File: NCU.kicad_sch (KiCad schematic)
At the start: 3 parts, among them J2 USB_C_Receptacle_USB2.0_14P

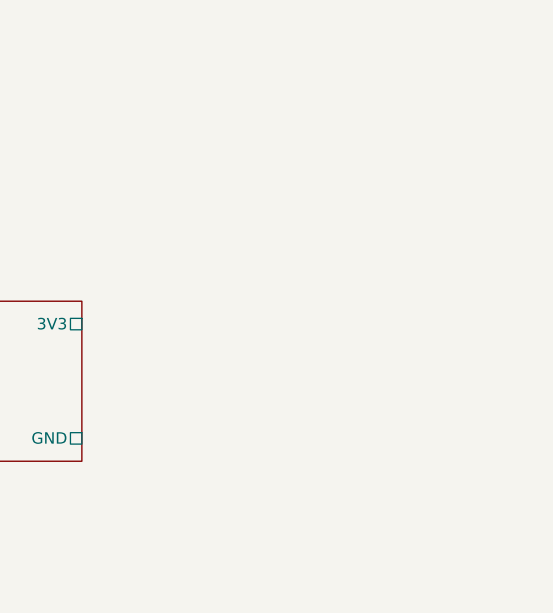
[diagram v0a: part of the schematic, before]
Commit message: added ethernet chip
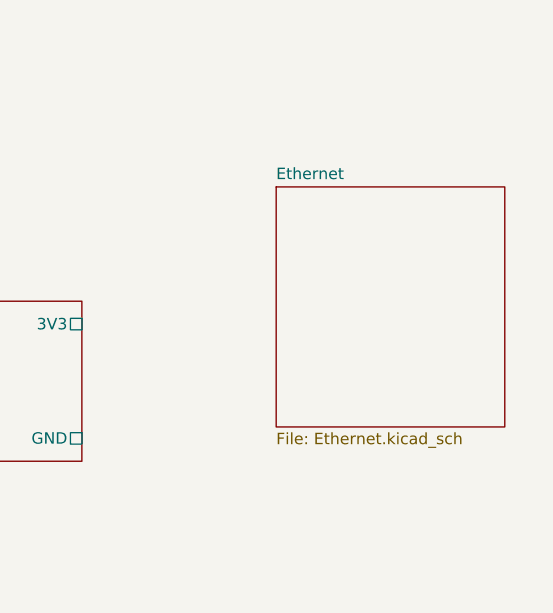
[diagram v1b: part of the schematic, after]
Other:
- added sheet Ethernet (Ethernet.kicad_sch)
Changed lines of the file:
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@@
+	)
+	(sheet
+		(at 228.6 63.5)
+		(size 25.4 26.67)
+		(exclude_from_sim no)
+		(in_bom yes)
+		(on_board yes)
+		(dnp no)
+		(fields_autoplaced yes)
+		(stroke
+			(width 0.1524)
+			(type solid)
+		)
+		(fill
+			(color 0 0 0 0.0000)
+		)
+		(property "Sheetname" "Ethernet"
+			(at 228.6 62.7884 0)
+			(effects
+				(font
+					(size 1.27 1.27)
+				)
+				(justify left bottom)
+			)
+		)
+		(property "Sheetfile" "Ethernet.kicad_sch"
+			(at 228.6 90.7546 0)
+			(effects
+				(font
+					(size 1.27 1.27)
+				)
+				(justify left top)
+			)
+		)
+		(instances
+			(project "NCU"
+				(path "/3aee14c3-5480-4f7c-989e-3fef81779034"
+					(page "8")
+				)
+			)
+		)
 	)
 	(sheet

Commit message: wip
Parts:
- removed J2: USB_C_Receptacle_USB2.0_14P, Connector_USB:USB_C_Receptacle_GCT_USB4110, symbol Connector:USB_C_Receptacle_USB2.0_14P
- removed R1, R2: 5K1, symbol Device:R
- added J1: RJ45, Connector_RJ:RJ45_Hanrun_HR911105A_Horizontal, symbol Connector:RJ45
- added J2: USB_B, symbol Connector:USB_B
- added J3: Micro_SD_Card, Connector_Card:microSD_HC_Molex_47219-2001, symbol Connector:Micro_SD_Card
- added J4: USB_C_Receptacle, symbol Connector:USB_C_Receptacle
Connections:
- net +5V: now also J2.1 (VBUS)
- net GND: now also J2.4 (GND), J2.5 (Shield), J3.9 (SHIELD)
- net USB/D+: now also J2.2 (D-)
- net USB/D-: now also J2.3 (D+)
- new net: J4.A1 (GND), J4.A12 (GND), J4.B1 (GND), J4.B12 (GND)
- new net: J4.A4 (VBUS), J4.A9 (VBUS), J4.B4 (VBUS), J4.B9 (VBUS)
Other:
- sheet Wireless Module renamed WiFi Bluetooth Module
- added sheet Cellular Module (CellularModule.kicad_sch)
- sheet WiFi Bluetooth Module: file WirelessModule.kicad_sch -> WifiBluetoothModule.kicad_sch

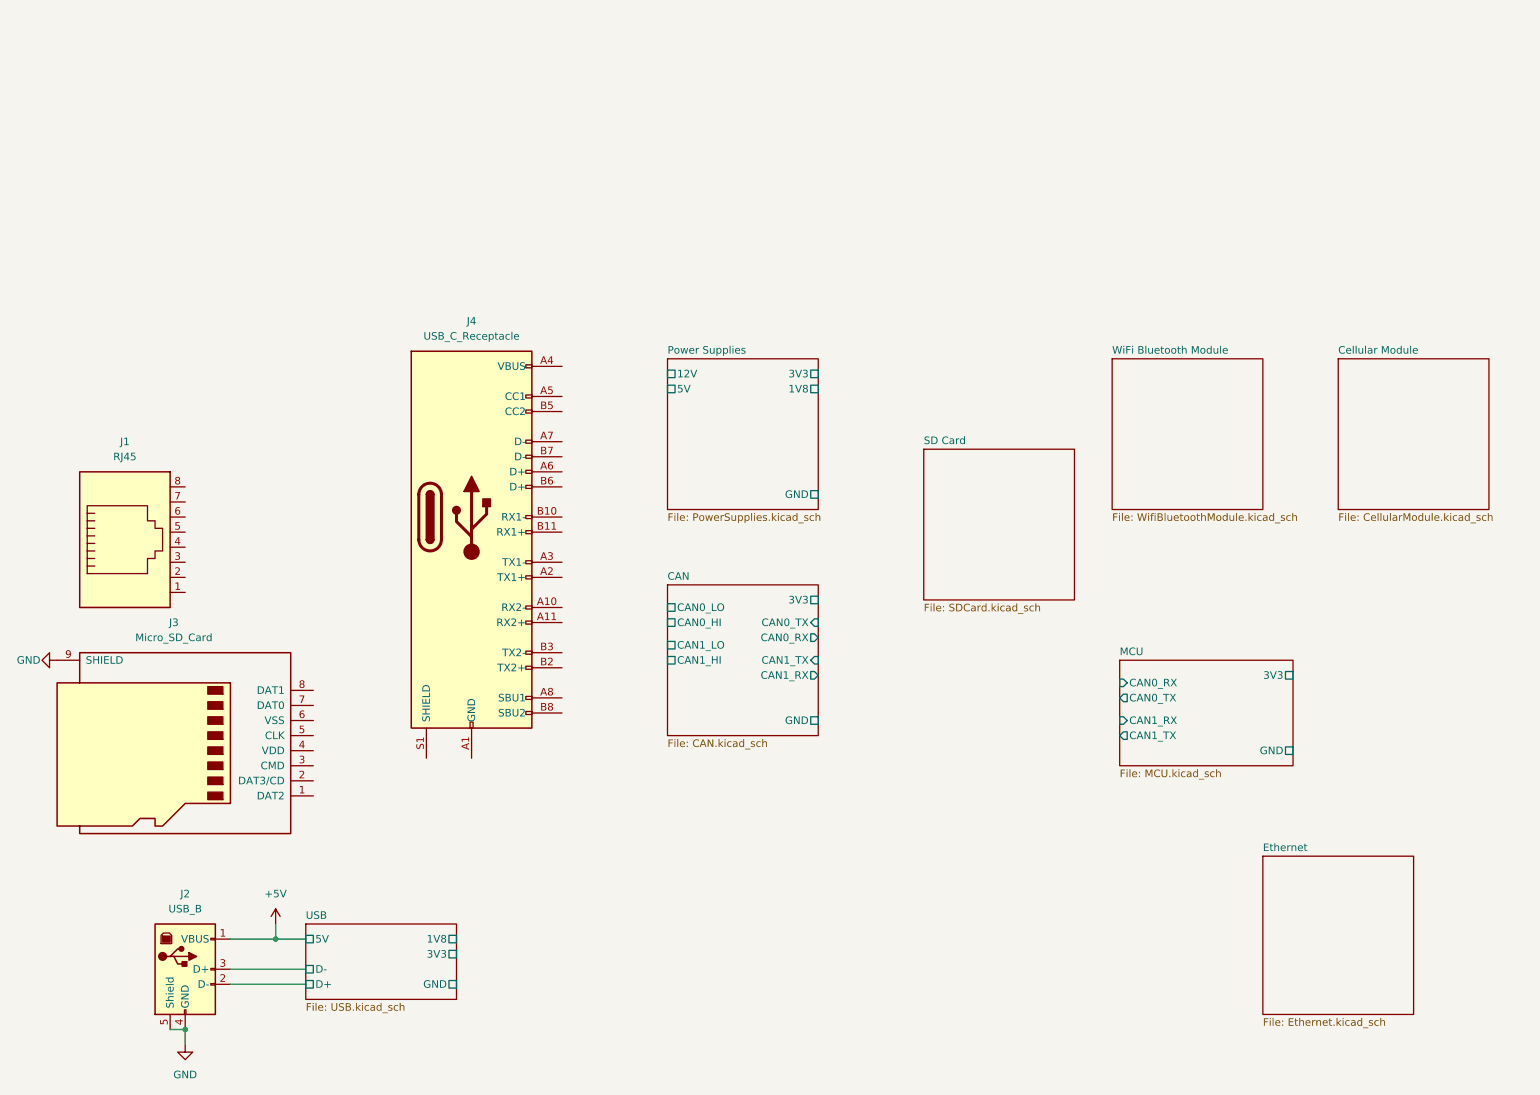
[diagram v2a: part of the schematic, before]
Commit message: updated to use RMII and routed ethernet and CAN from micro
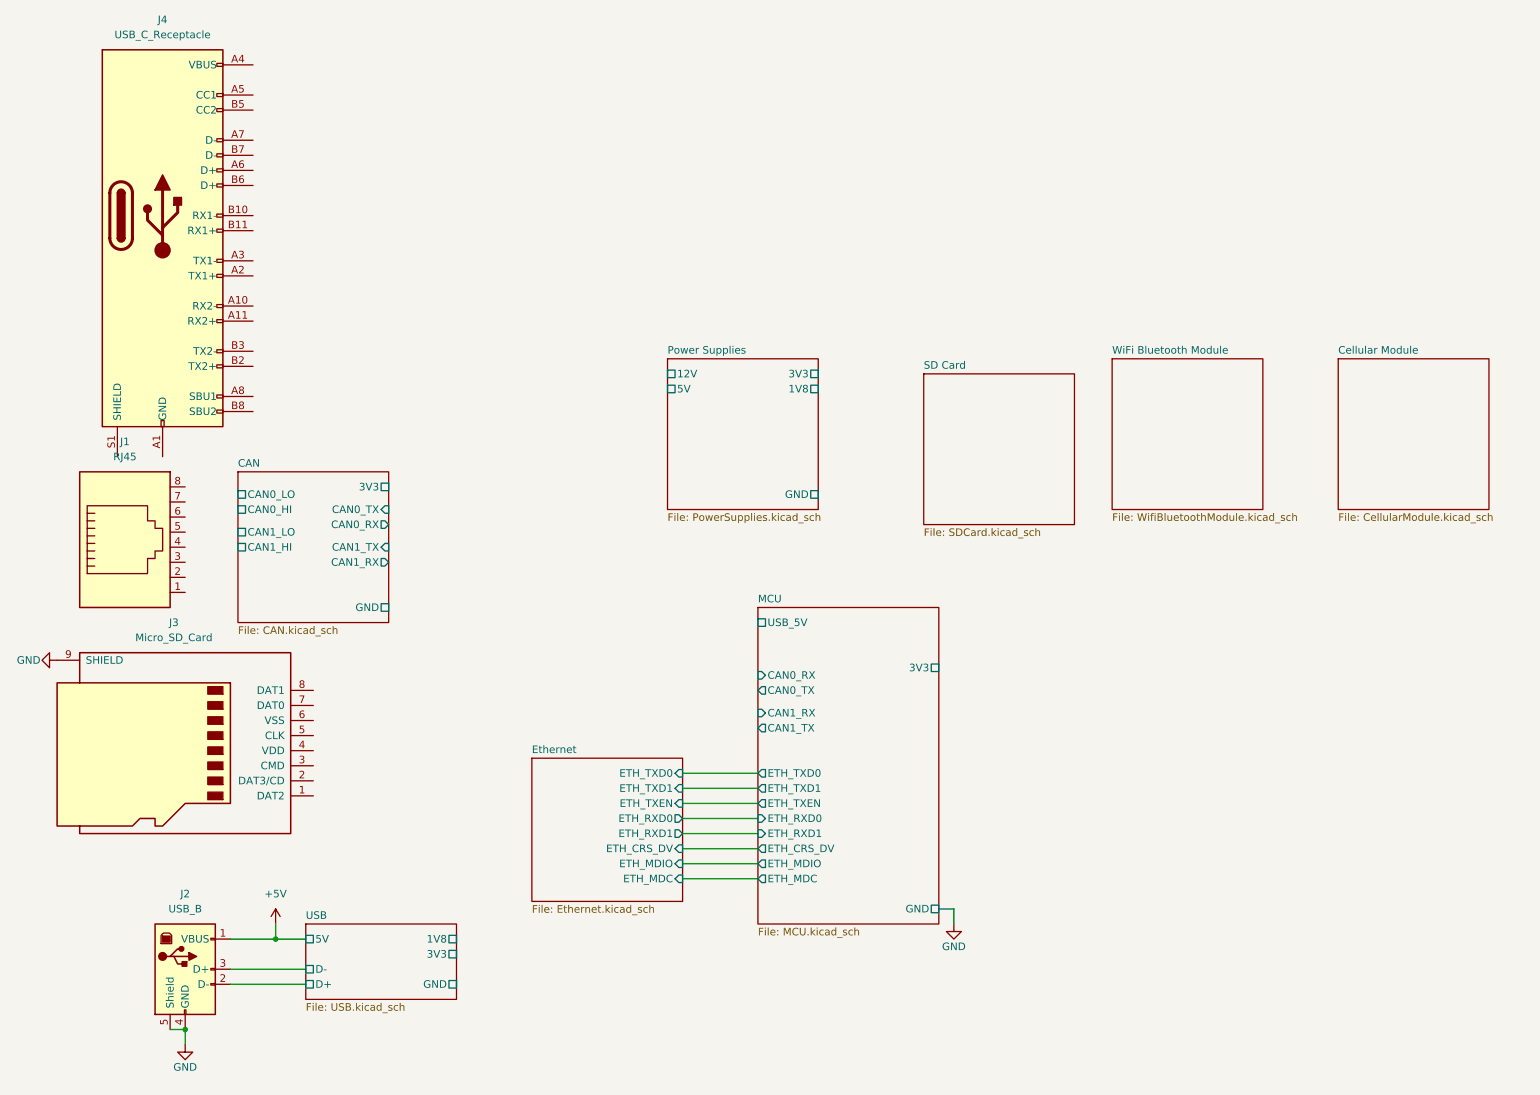
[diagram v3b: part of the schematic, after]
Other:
- sheet Ethernet ports: added ETH_CRS_DV, ETH_MDC, ETH_MDIO, ETH_RXD0, ETH_RXD1, ETH_TXD0, ETH_TXD1, ETH_TXEN; removed none
- sheet MCU ports: added ETH_CRS_DV, ETH_MDC, ETH_MDIO, ETH_RXD0, ETH_RXD1, ETH_TXD0, ETH_TXD1, ETH_TXEN, USB_5V; removed none
- moved on the sheet: J4

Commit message: wip
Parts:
- removed J4: USB_C_Receptacle, symbol Connector:USB_C_Receptacle
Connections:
- net USB/D+ renamed MCU/USB_DM
- net USB/D- renamed MCU/USB_DP
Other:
- removed sheet USB
- sheet MCU ports: added USB_DM, USB_DP, USB_VBUS; removed none
- moved on the sheet: J2

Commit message: full initial power scheme
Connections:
- net MCU/USB_DM: no longer J2.2 (D-)
- net MCU/USB_DP: no longer J2.3 (D+)
- net +5V renamed USB_5V
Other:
- sheet MCU ports: added none; removed USB_5V
- sheet Power Supplies ports: added USB_5V; removed 1V8
- moved on the sheet: J1, J2, J3

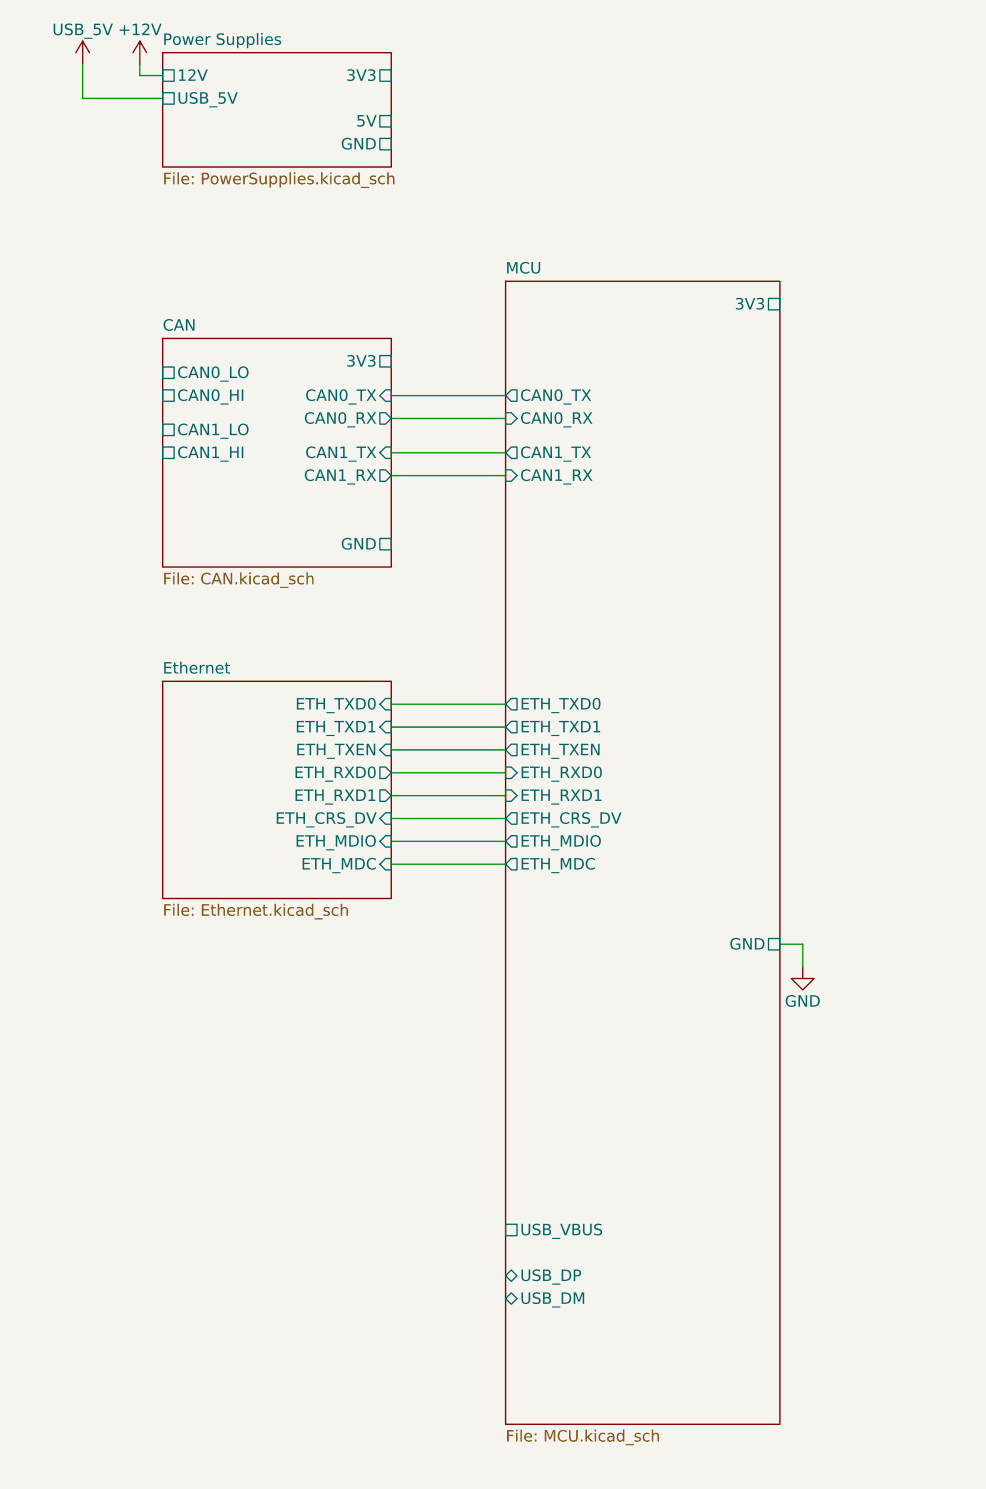
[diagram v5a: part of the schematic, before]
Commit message: improved power supplies, added ADCs
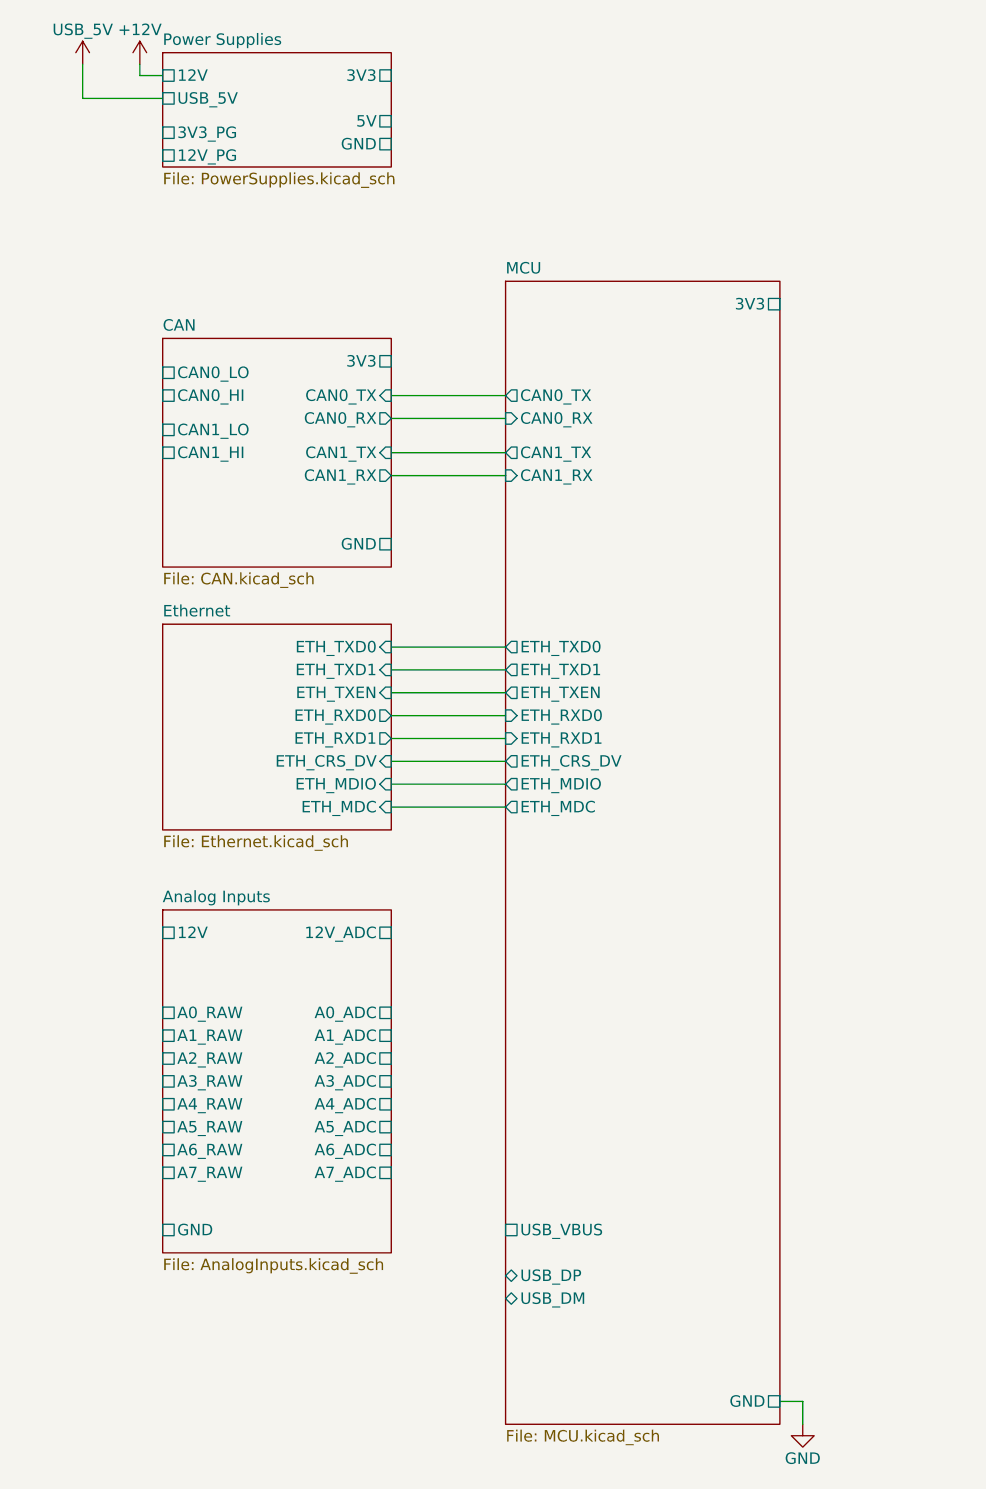
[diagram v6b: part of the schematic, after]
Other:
- added sheet Analog Inputs (AnalogInputs.kicad_sch)
- sheet Power Supplies ports: added 12V_PG, 3V3_PG; removed none

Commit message: wip
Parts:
- J2: footprint (none) -> Connector_USB:USB_B_Lumberg_2411_02_Horizontal
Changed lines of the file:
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@@
 			)
 		)
-		(property "Footprint" ""
+		(property "Footprint" "Connector_USB:USB_B_Lumberg_2411_02_Horizontal"
 			(at 34.29 59.69 0)
 			(effects
